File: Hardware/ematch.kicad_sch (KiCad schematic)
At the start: 33 parts, among them J3 Conn_01x02_Male, J4 Conn_01x02_Male, J5 Conn_01x02_Male, J6 Conn_01x02_Male, Q1 BUK9M11-40EX, Q2 BUK9M11-40EX, Q3 BUK9M11-40EX, Q4 BUK9M11-40EX, U6 LTV-247

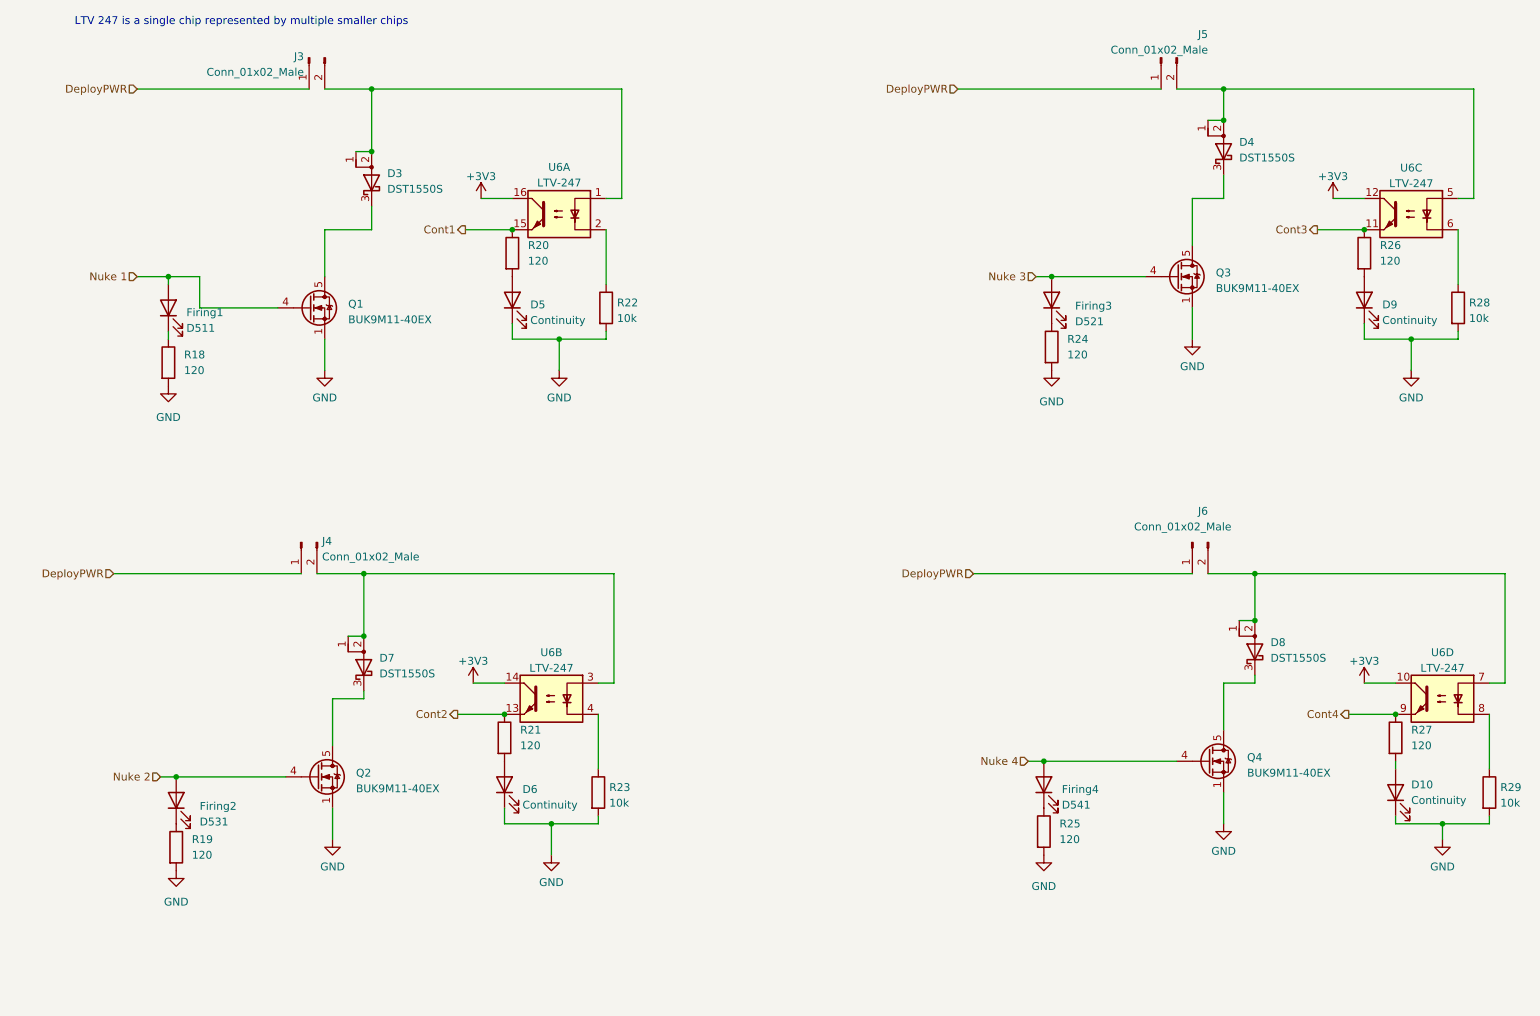
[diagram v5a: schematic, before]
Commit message: mostly finished new power layout, needs some vias and i2c routing
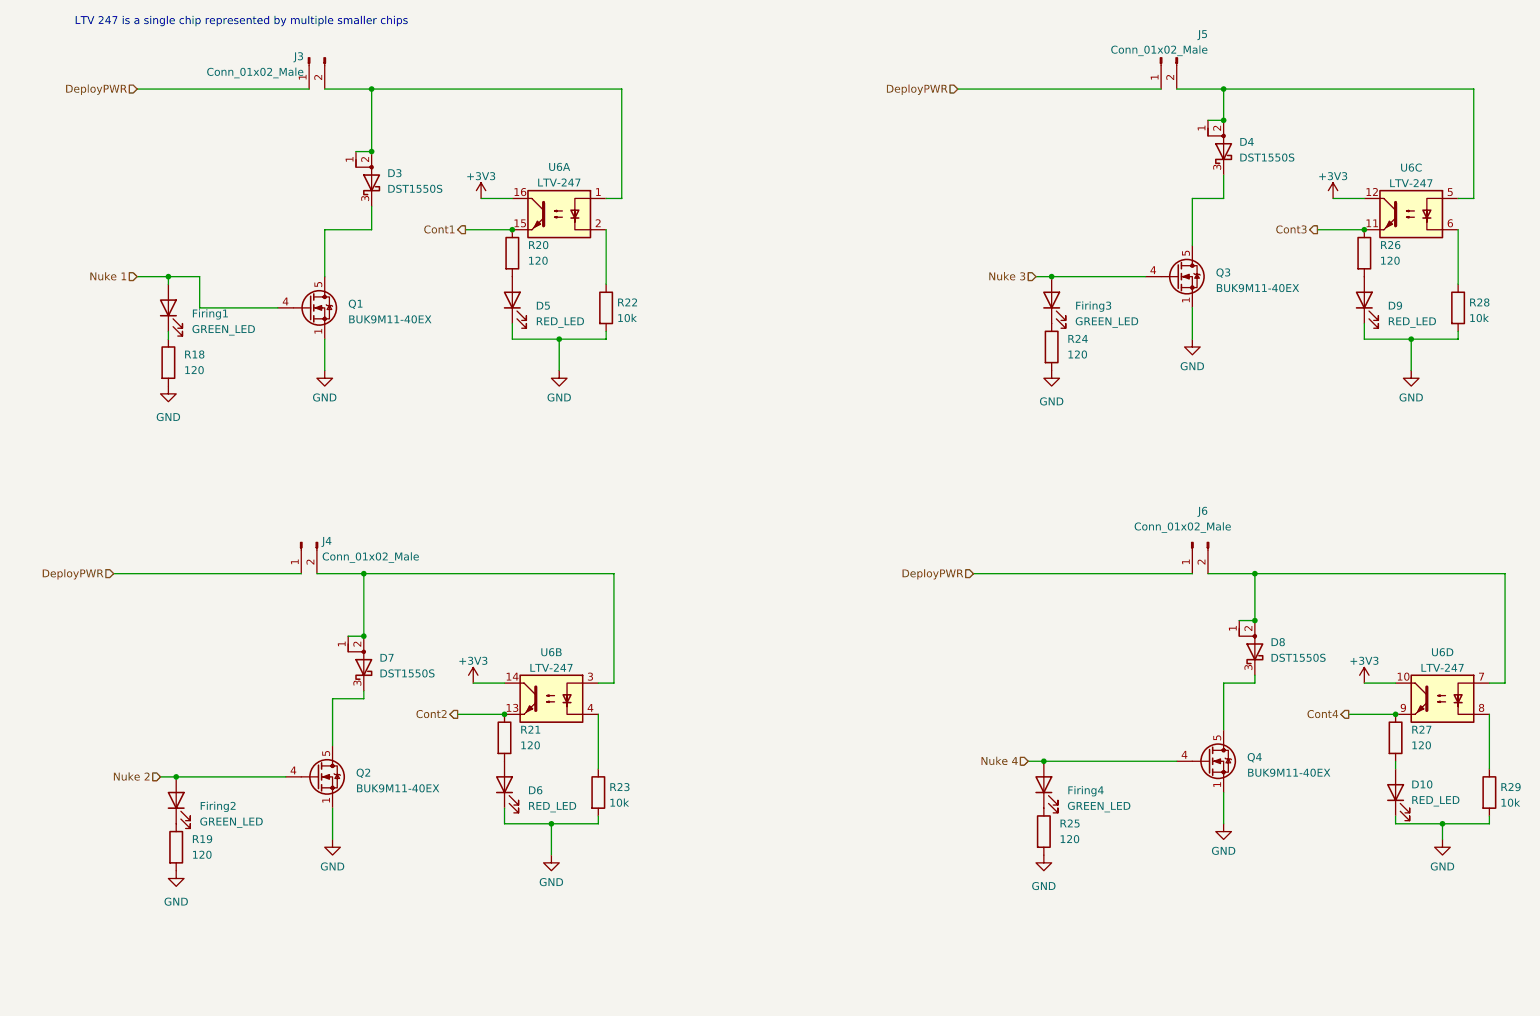
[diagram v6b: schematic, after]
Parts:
- D10, D5, D6, D9: value Continuity -> RED_LED
- Firing1: value D511 -> GREEN_LED; footprint LED_SMD:LED_0603_1608Metric -> LED_SMD:LED_0402_1005Metric
- Firing2: value D531 -> GREEN_LED; footprint LED_SMD:LED_0603_1608Metric -> LED_SMD:LED_0402_1005Metric
- Firing3: value D521 -> GREEN_LED; footprint LED_SMD:LED_0603_1608Metric -> LED_SMD:LED_0402_1005Metric
- Firing4: value D541 -> GREEN_LED; footprint LED_SMD:LED_0603_1608Metric -> LED_SMD:LED_0402_1005Metric
- R18, R19, R24, R25: footprint Resistor_SMD:R_0603_1608Metric -> Resistor_SMD:R_0402_1005Metric
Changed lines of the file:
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@@
   (symbol (lib_id "Device:LED") (at 179.07 143.51 90) (unit 1)
     (in_bom yes) (on_board yes) (dnp no) (fields_autoplaced)
-    (property "Reference" "Firing4" (at 181.991 144.2628 90)
-      (effects (font (size 1.27 1.27)) (justify right))
-    )
-    (property "Value" "D541" (at 181.991 146.7997 90)
-      (effects (font (size 1.27 1.27)) (justify right))
-    )
-    (property "Footprint" "LED_SMD:LED_0603_1608Metric" (at 179.07 143.51 0)
+    (property "Reference" "Firing4" (at 182.88 144.4625 90)
+      (effects (font (size 1.27 1.27)) (justify right))
+    )
+    (property "Value" "GREEN_LED" (at 182.88 147.0025 90)
+      (effects (font (size 1.27 1.27)) (justify right))
+    )
+    (property "Footprint" "LED_SMD:LED_0402_1005Metric" (at 179.07 143.51 0)
       (effects (font (size 1.27 1.27)) hide)
     )
@@
       (effects (font (size 1.27 1.27)) (justify right))
     )
-    (property "Value" "Continuity" (at 238.76 146.05 90)
+    (property "Value" "RED_LED" (at 238.76 146.05 90)
       (effects (font (size 1.27 1.27)) (justify right))
     )
@@
   (symbol (lib_id "Device:LED") (at 36.83 66.04 90) (unit 1)
     (in_bom yes) (on_board yes) (dnp no) (fields_autoplaced)
-    (property "Reference" "Firing1" (at 39.751 66.7928 90)
-      (effects (font (size 1.27 1.27)) (justify right))
-    )
-    (property "Value" "D511" (at 39.751 69.3297 90)
-      (effects (font (size 1.27 1.27)) (justify right))
-    )
-    (property "Footprint" "LED_SMD:LED_0603_1608Metric" (at 36.83 66.04 0)
+    (property "Reference" "Firing1" (at 40.64 66.9925 90)
+      (effects (font (size 1.27 1.27)) (justify right))
+    )
+    (property "Value" "GREEN_LED" (at 40.64 69.5325 90)
+      (effects (font (size 1.27 1.27)) (justify right))
+    )
+    (property "Footprint" "LED_SMD:LED_0402_1005Metric" (at 36.83 66.04 0)
       (effects (font (size 1.27 1.27)) hide)
     )
@@
       (effects (font (size 1.27 1.27)) (justify left))
     )
-    (property "Footprint" "Resistor_SMD:R_0603_1608Metric" (at 178.562 72.39 90)
+    (property "Footprint" "Resistor_SMD:R_0402_1005Metric" (at 178.562 72.39 90)
       (effects (font (size 1.27 1.27)) hide)
     )
@@
       (effects (font (size 1.27 1.27)) (justify right))
     )
-    (property "Value" "D531" (at 41.91 149.5425 90)
-      (effects (font (size 1.27 1.27)) (justify right))
-    )
-    (property "Footprint" "LED_SMD:LED_0603_1608Metric" (at 38.1 146.05 0)
+    (property "Value" "GREEN_LED" (at 41.91 149.5425 90)
+      (effects (font (size 1.27 1.27)) (justify right))
+    )
+    (property "Footprint" "LED_SMD:LED_0402_1005Metric" (at 38.1 146.05 0)
       (effects (font (size 1.27 1.27)) hide)
     )
@@
       (effects (font (size 1.27 1.27)) (justify left))
     )
-    (property "Footprint" "Resistor_SMD:R_0603_1608Metric" (at 177.292 151.13 90)
+    (property "Footprint" "Resistor_SMD:R_0402_1005Metric" (at 177.292 151.13 90)
       (effects (font (size 1.27 1.27)) hide)
     )
@@
   (symbol (lib_id "Device:LED") (at 92.71 64.77 90) (unit 1)
     (in_bom yes) (on_board yes) (dnp no) (fields_autoplaced)
-    (property "Reference" "D5" (at 95.631 65.5228 90)
-      (effects (font (size 1.27 1.27)) (justify right))
-    )
-    (property "Value" "Continuity" (at 95.631 68.0597 90)
+    (property "Reference" "D5" (at 96.52 65.7225 90)
+      (effects (font (size 1.27 1.27)) (justify right))
+    )
+    (property "Value" "RED_LED" (at 96.52 68.2625 90)
       (effects (font (size 1.27 1.27)) (justify right))
     )
@@
   (symbol (lib_id "Device:LED") (at 231.14 64.77 90) (unit 1)
     (in_bom yes) (on_board yes) (dnp no) (fields_autoplaced)
-    (property "Reference" "D9" (at 234.061 65.5228 90)
-      (effects (font (size 1.27 1.27)) (justify right))
-    )
-    (property "Value" "Continuity" (at 234.061 68.0597 90)
+    (property "Reference" "D9" (at 234.95 65.7225 90)
+      (effects (font (size 1.27 1.27)) (justify right))
+    )
+    (property "Value" "RED_LED" (at 234.95 68.2625 90)
       (effects (font (size 1.27 1.27)) (justify right))
     )
@@
       (effects (font (size 1.27 1.27)) (justify left))
     )
-    (property "Footprint" "Resistor_SMD:R_0603_1608Metric" (at 35.052 74.93 90)
+    (property "Footprint" "Resistor_SMD:R_0402_1005Metric" (at 35.052 74.93 90)
       (effects (font (size 1.27 1.27)) hide)
     )
@@
       (effects (font (size 1.27 1.27)) (justify left))
     )
-    (property "Footprint" "Resistor_SMD:R_0603_1608Metric" (at 36.322 153.67 90)
+    (property "Footprint" "Resistor_SMD:R_0402_1005Metric" (at 36.322 153.67 90)
       (effects (font (size 1.27 1.27)) hide)
     )
@@
   (symbol (lib_id "Device:LED") (at 91.44 143.51 90) (unit 1)
     (in_bom yes) (on_board yes) (dnp no) (fields_autoplaced)
-    (property "Reference" "D6" (at 94.361 144.2628 90)
-      (effects (font (size 1.27 1.27)) (justify right))
-    )
-    (property "Value" "Continuity" (at 94.361 146.7997 90)
+    (property "Reference" "D6" (at 95.25 144.4625 90)
+      (effects (font (size 1.27 1.27)) (justify right))
+    )
+    (property "Value" "RED_LED" (at 95.25 147.0025 90)
       (effects (font (size 1.27 1.27)) (justify right))
     )
@@
       (effects (font (size 1.27 1.27)) (justify right))
     )
-    (property "Value" "D521" (at 184.15 68.2625 90)
-      (effects (font (size 1.27 1.27)) (justify right))
-    )
-    (property "Footprint" "LED_SMD:LED_0603_1608Metric" (at 180.34 64.77 0)
-      (effects (font (size 1.27 1.27)) hide)
-    )
+    (property "Value" "GREEN_LED" (at 184.15 68.2625 90)
+      (effects (font (size 1.27 1.27)) (justify right))
+    )
+    (property "Footprint" "LED_SMD:LED_0402_1005Metric" (at 180.34 64.77 0)
+      (effects (font (size 1.27 1.27)) hide)
+    )

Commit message: v2.1 ordering
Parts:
- Firing1, Firing2, Firing3, Firing4: value GREEN_LED -> EMERALD_LED
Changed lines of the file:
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@@
       (effects (font (size 1.27 1.27)) (justify right))
     )
-    (property "Value" "GREEN_LED" (at 182.88 147.0025 90)
+    (property "Value" "EMERALD_LED" (at 182.88 147.0025 90)
       (effects (font (size 1.27 1.27)) (justify right))
     )
@@
       (effects (font (size 1.27 1.27)) (justify right))
     )
-    (property "Value" "GREEN_LED" (at 40.64 69.5325 90)
+    (property "Value" "EMERALD_LED" (at 40.64 69.5325 90)
       (effects (font (size 1.27 1.27)) (justify right))
     )
@@
       (effects (font (size 1.27 1.27)) (justify right))
     )
-    (property "Value" "GREEN_LED" (at 41.91 149.5425 90)
+    (property "Value" "EMERALD_LED" (at 41.91 149.5425 90)
       (effects (font (size 1.27 1.27)) (justify right))
     )
@@
       (effects (font (size 1.27 1.27)) (justify right))
     )
-    (property "Value" "GREEN_LED" (at 184.15 68.2625 90)
-      (effects (font (size 1.27 1.27)) (justify right))
-    )
+    (property "Value" "EMERALD_LED" (at 184.15 68.2625 90)
+      (effects (font (size 1.27 1.27)) (justify right))
+    )
